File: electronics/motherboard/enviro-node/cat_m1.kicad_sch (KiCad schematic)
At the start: 38 parts, among them J11 CONUFL001-SMD-T, J12 SIM8060-6-0-14-00-A, Q4 BC847, Q5 BC847, SW3 CAT_M1_RST, U11 TPS22967DSGR, U12 SARA-R410M-02B, U13 TXB0104PW

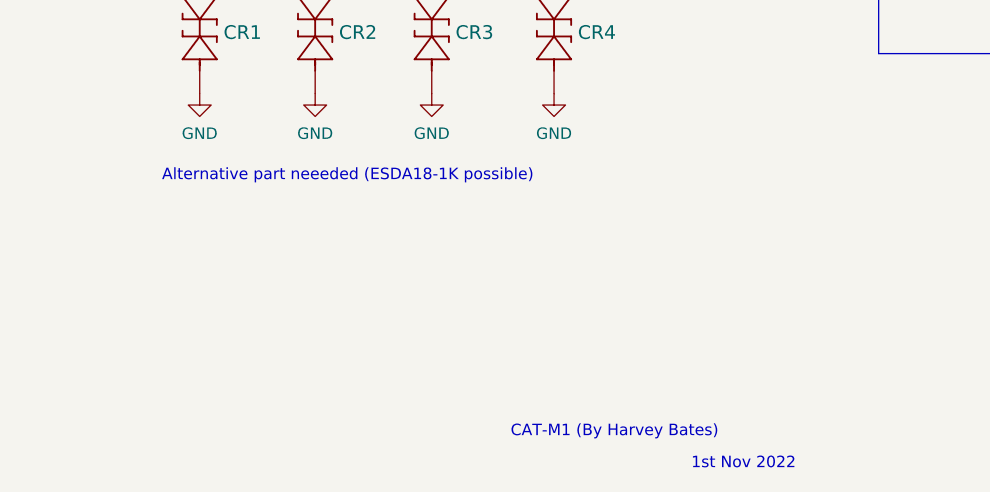
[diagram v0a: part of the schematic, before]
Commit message: fixed unexposed copper pad on inductor and added zipped step file of the motherboard
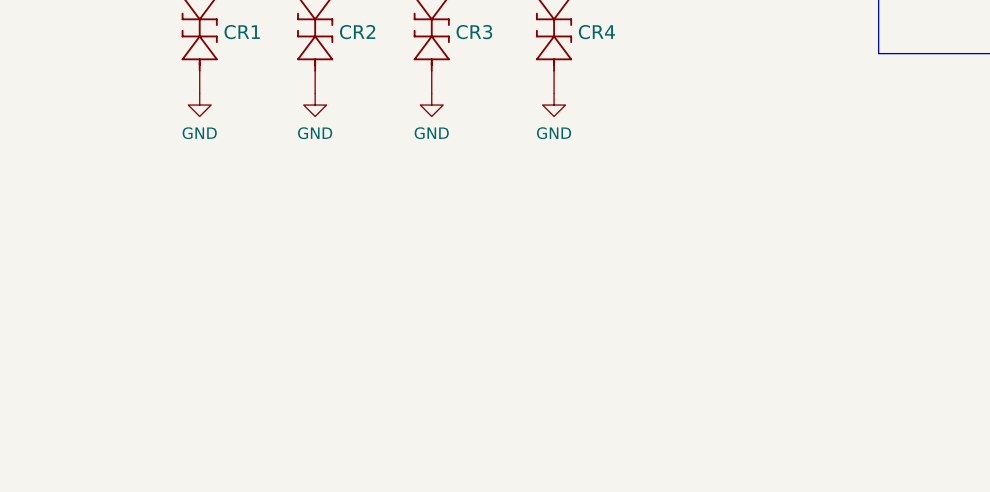
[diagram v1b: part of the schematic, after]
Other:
- note removed: "1st Nov 2022"
- note removed: "Alternative part neeeded (ESDA18-1K possible)"
- note removed: "CAT-M1 (By Harvey Bates)"
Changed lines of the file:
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@@
     (effects (font (size 1.27 1.27)) (justify right bottom))
-  )
-  (text "Alternative part neeeded (ESDA18-1K possible)" (at 148.336 162.179 0)
-    (effects (font (size 1.27 1.27)) (justify left bottom))
-  )
-  (text "1st Nov 2022" (at 207.137 194.183 0)
-    (effects (font (size 1.27 1.27)) (justify left bottom))
-  )
-  (text "CAT-M1 (By Harvey Bates)" (at 187.071 190.627 0)
-    (effects (font (size 1.27 1.27)) (justify left bottom))
   )
   (text "CAT-M1 Modem" (at 87.376 84.963 0)

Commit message: updated electronics for production
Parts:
- U12: value SARA-R410M-02B -> SARA-R500S-01B; Part SARA-R410M-02B -> SARA-R500S-01B
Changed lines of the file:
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@@
     (in_bom yes) (on_board yes) (fields_autoplaced)
     (property "Reference" "U12" (id 0) (at 98.552 98.7892 0))
-    (property "Value" "SARA-R410M-02B" (id 1) (at 98.552 101.3261 0))
+    (property "Value" "SARA-R500S-01B" (id 1) (at 98.552 101.3261 0))
     (property "Footprint" "SARA-R410M-02B:XCVR_SARA-R410M-02B" (id 2) (at 98.552 140.589 0)
       (effects (font (size 1.27 1.27)) (justify left bottom) hide)
@@
       (effects (font (size 1.27 1.27)) (justify left bottom) hide)
     )
-    (property "Part" "SARA-R410M-02B" (id 4) (at 98.552 140.589 0)
+    (property "Part" "SARA-R500S-01B" (id 4) (at 98.552 140.589 0)
       (effects (font (size 1.27 1.27)) hide)
     )

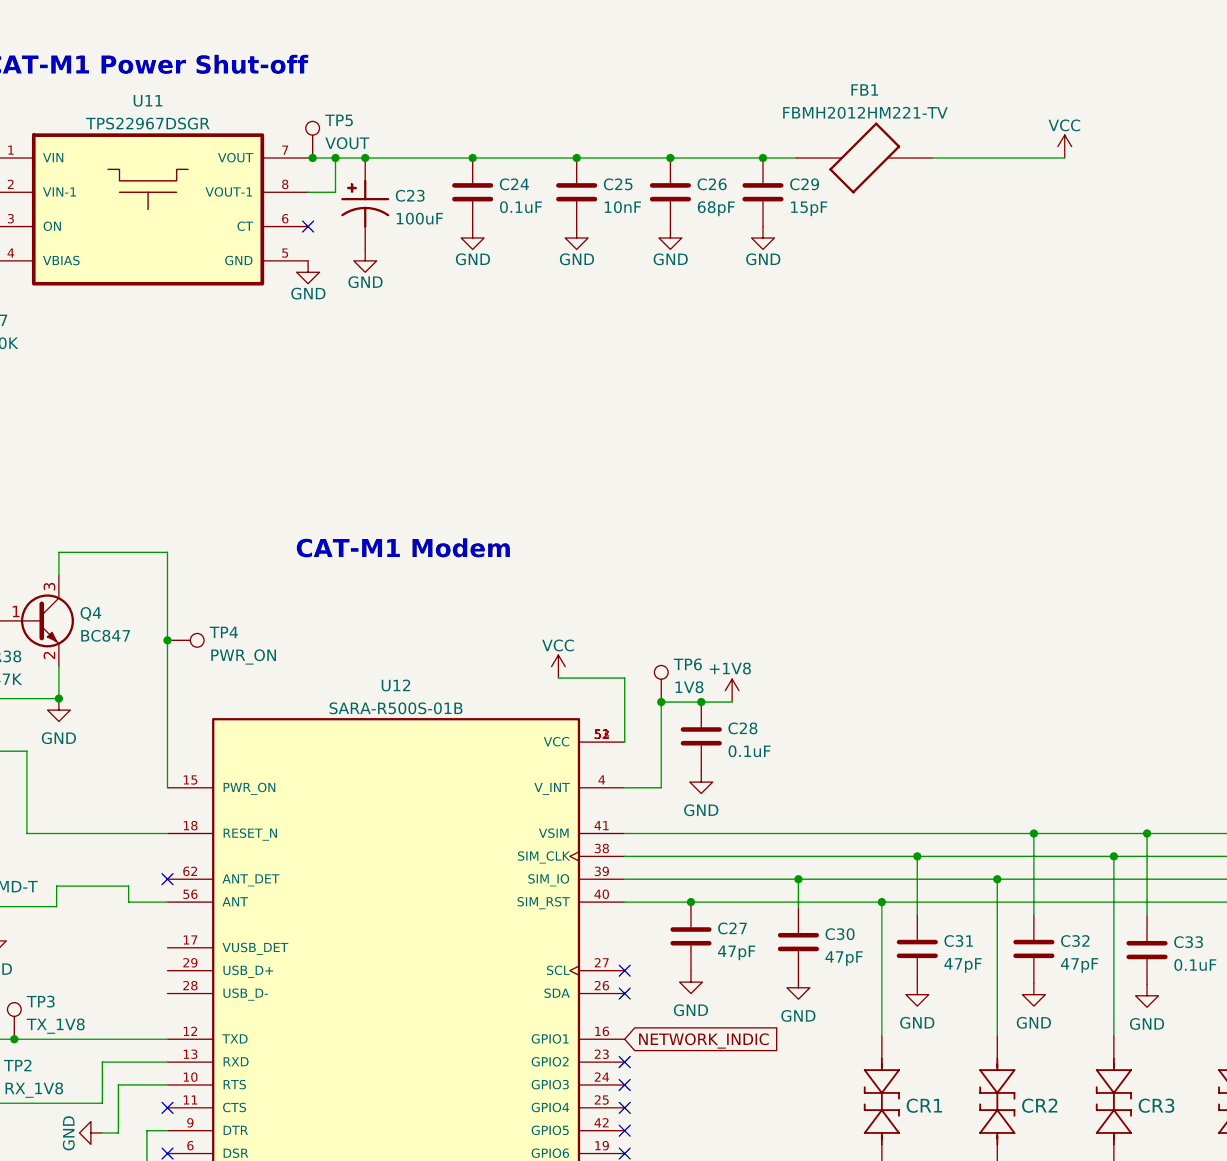
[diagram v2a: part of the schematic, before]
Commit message: Fixed most errors on the 1.0.1 board revision, resolved ERC errors. No PCB work in this commit.
1. Added a solder jumper in-line with with the USB/UART bridge TX pin. If this jumper is
   broken then the RX pin on the UART header can be used. Note the TX/RX discrepancy here is
   not a typo.

2. Changed the USB/UART bridge power supply wiring so it will not try to power the board
   when a USB cable is plugged in. Batteries must be present.

3. The battery monitor VS/A0/A1 pins put back to +3.3v rather than VBAT so it can be read
   while the battery is being charged via the solar panel.

4. Moved the main 3.3v regulator to after the power switch so it is not running all the time.

5. Reverted the change that swapped the piezo buzzer and rain gauge input pins.

6. Noted that R42 and R43 should not be populated during manufacture.

7. Changed the part number for the USB-C LiPo charger to MCP73832T-2ACI/OT.

8. Resolved all KiCAD ERC errors on the schematics. These were all related to KiCAD not
   knowing where power was coming from or IC power pins not being correctly defined in
   the components. Warnings were not checked.
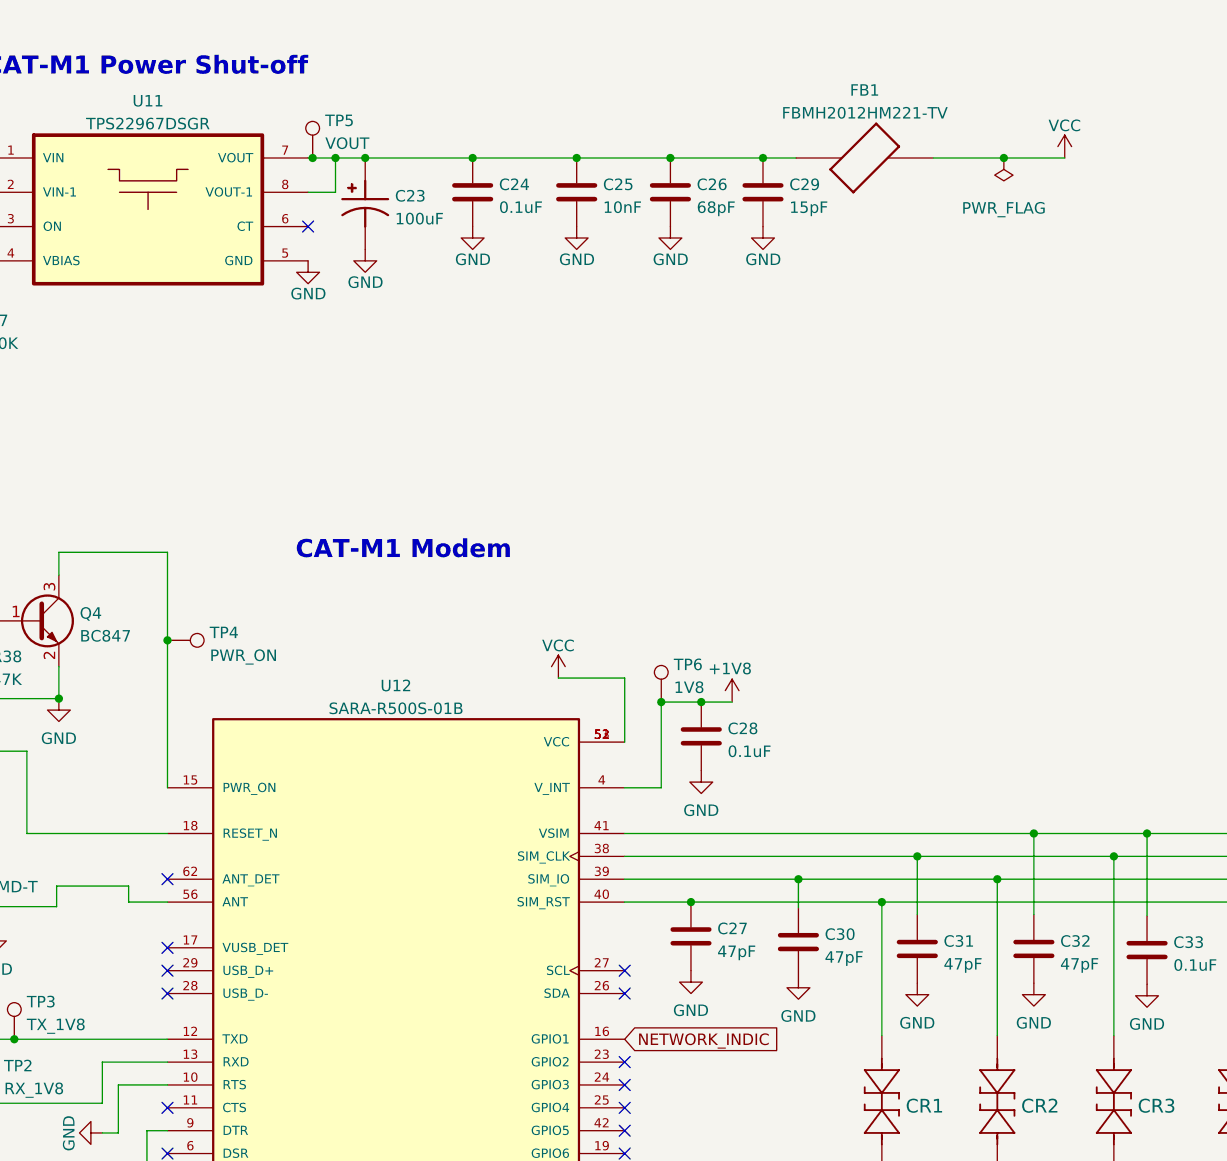
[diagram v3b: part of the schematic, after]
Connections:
- no-connect marks 32 -> 35
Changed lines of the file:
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@@
   (junction (at 165.354 120.269) (diameter 0) (color 0 0 0 0)
+  )
+  (junction (at 166.0824 40.132) (diameter 0) (color 0 0 0 0)
   )
   (junction (at 50.8 40.132) (diameter 0) (color 0 0 0 0)
@@
   (no_connect (at 123.952 165.989))
   (no_connect (at 220.345 56.769))
+  (no_connect (at 73.152 132.969))
+  (no_connect (at 73.152 127.889))
+  (no_connect (at 73.152 130.429))
   (no_connect (at 73.152 173.609))
   (no_connect (at 216.027 122.809))
@@
     (stroke (width 0) (type default) (color 0 0 0 0))
   )
-  (wire (pts (xy 158.242 40.132) (xy 172.847 40.132))
+  (wire (pts (xy 158.242 40.132) (xy 166.0824 40.132))
     (stroke (width 0) (type default) (color 0 0 0 0))
   )
@@
   )
   (wire (pts (xy 132.461 100.584) (xy 135.89 100.584))
+    (stroke (width 0) (type default) (color 0 0 0 0))
+  )
+  (wire (pts (xy 166.0824 40.132) (xy 172.847 40.132))
     (stroke (width 0) (type default) (color 0 0 0 0))
   )
@@
       (effects (font (size 1.27 1.27)) hide)
     )
+    (pin "1")
+  )
+  (symbol (lib_id "power:PWR_FLAG") (at 166.0824 40.132 180) (unit 1)
+    (in_bom yes) (on_board yes) (fields_autoplaced)
+    (property "Reference" "#FLG0101" (id 0) (at 166.0824 42.037 0)
+      (effects (font (size 1.27 1.27)) hide)
+    )
+    (property "Value" "PWR_FLAG" (id 1) (at 166.0824 45.72 0))
+    (property "Footprint" "" (id 2) (at 166.0824 40.132 0)
+      (effects (font (size 1.27 1.27)) hide)
+    )
+    (property "Datasheet" "~" (id 3) (at 166.0824 40.132 0)
+      (effects (font (size 1.27 1.27)) hide)
+    )

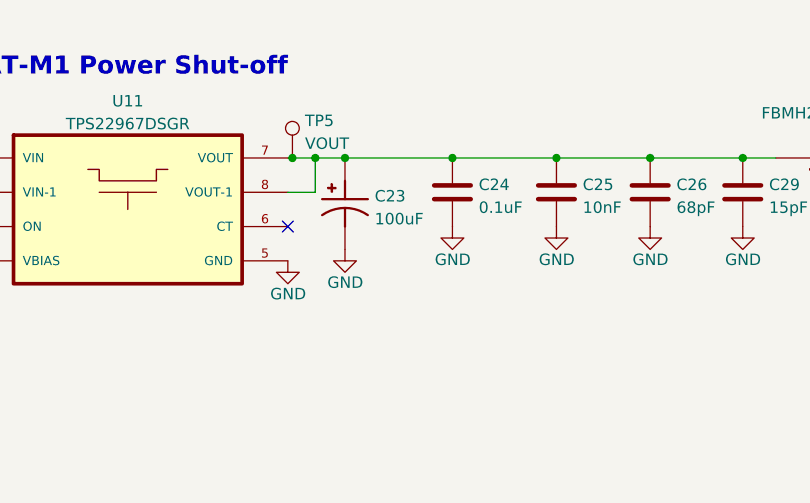
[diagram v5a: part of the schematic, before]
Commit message: Last commit did not get changes to C17 & C23, changed them again to 0.1uF.
Changed footprint of optional pull-up/pull-down R42 & R43 to be through-hole.
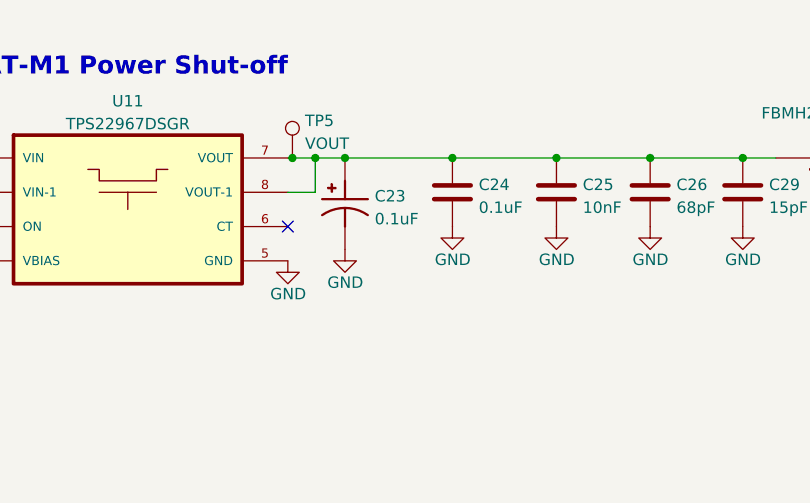
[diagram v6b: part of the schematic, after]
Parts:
- C23: value 100uF -> 0.1uF; footprint T520B107M006ATE015:CAPPM3528X210N -> Capacitor_Tantalum_SMD:CP_EIA-2012-12_Kemet-R; MANUFACTURER KEMET -> KYOCERA-AVX; Part T520B107M006ATE015 -> TAJR104K020RNJ
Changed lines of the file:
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@@
       (effects (font (size 1.27 1.27)) (justify left))
     )
-    (property "Value" "100uF" (id 1) (at 98.425 46.9142 90)
+    (property "Value" "0.1uF" (id 1) (at 98.425 46.9142 90)
       (effects (font (size 1.27 1.27)) (justify left))
     )
-    (property "Footprint" "T520B107M006ATE015:CAPPM3528X210N" (id 2) (at 95.123 45.212 0)
+    (property "Footprint" "Capacitor_Tantalum_SMD:CP_EIA-2012-12_Kemet-R" (id 2) (at 95.123 45.212 0)
       (effects (font (size 1.27 1.27)) (justify left bottom) hide)
     )
-    (property "Datasheet" "https://www.digikey.com.au/en/products/detail/kemet/T520B107M006ATE015/1842096?s=N4IgTCBcDaICoFYwAYBCBGZB2Ass5AbAIJwCiy6CIAugL5A" (id 3) (at 95.123 45.212 0)
+    (property "Datasheet" "https://datasheets.kyocera-avx.com/TAJ.pdf" (id 3) (at 95.123 45.212 0)
       (effects (font (size 1.27 1.27)) (justify left bottom) hide)
     )
@@
       (effects (font (size 1.27 1.27)) (justify left bottom) hide)
     )
-    (property "MANUFACTURER" "KEMET" (id 5) (at 95.123 45.212 0)
+    (property "MANUFACTURER" "KYOCERA-AVX" (id 5) (at 95.123 45.212 0)
       (effects (font (size 1.27 1.27)) (justify left bottom) hide)
     )
-    (property "Part" "T520B107M006ATE015" (id 6) (at 95.123 45.212 90)
+    (property "Part" "TAJR104K020RNJ" (id 6) (at 95.123 45.212 90)
       (effects (font (size 1.27 1.27)) hide)
     )

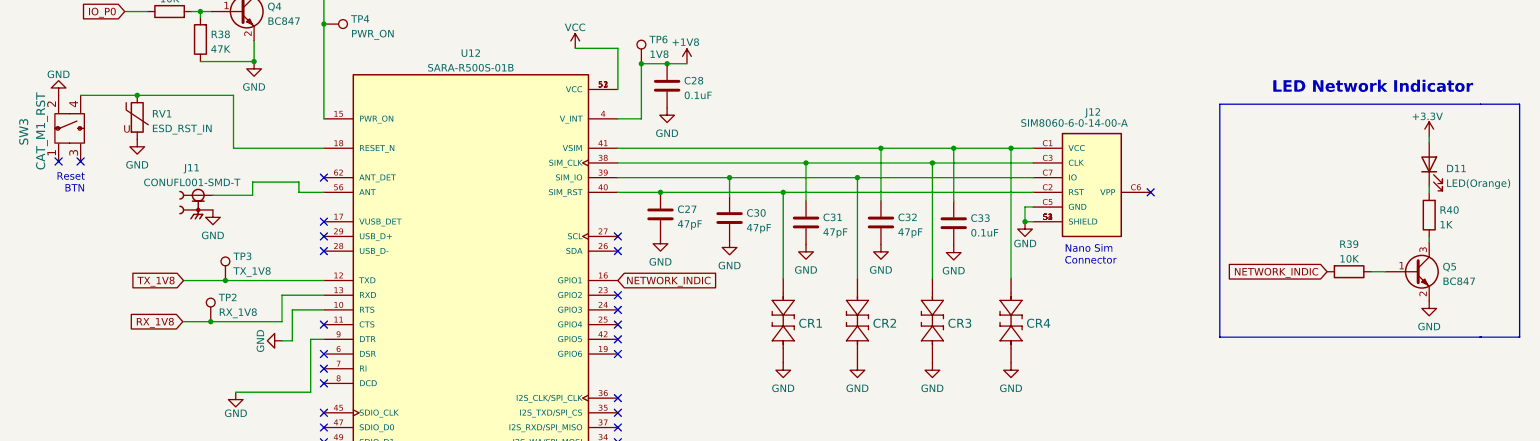
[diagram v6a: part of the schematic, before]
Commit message: v1.0.3, added TMP1075 temp sensor, now using kicad 8.
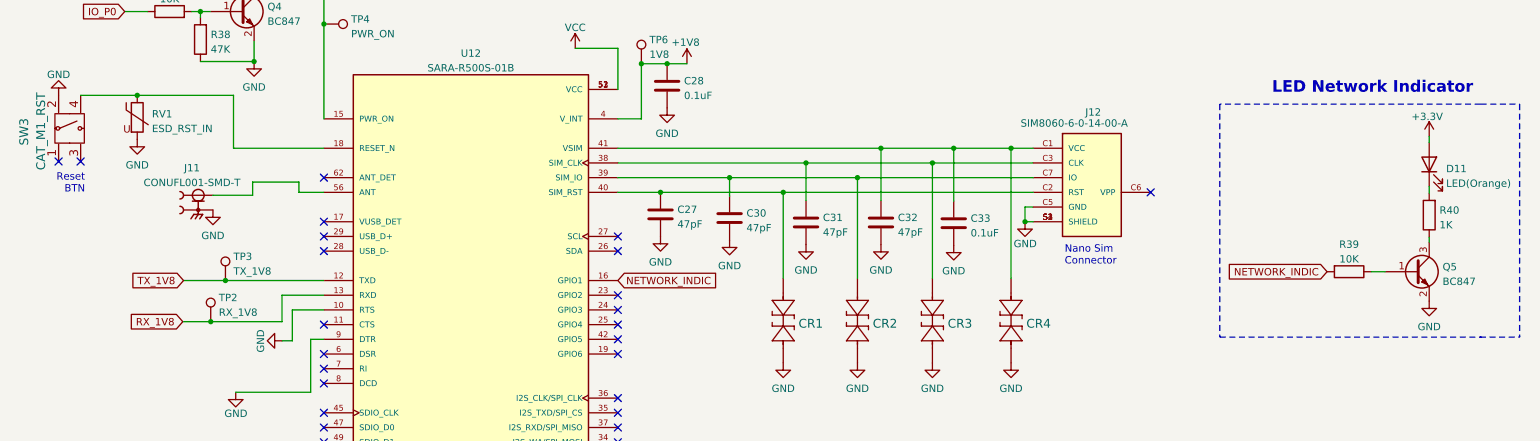
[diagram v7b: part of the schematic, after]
